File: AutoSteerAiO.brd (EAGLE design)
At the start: 114.3 x 99.1 mm, 82 parts, among them IC2 MMA8452Q, J4 CONNECTOR 1x5 PINS, K4 CB1A-P-12V

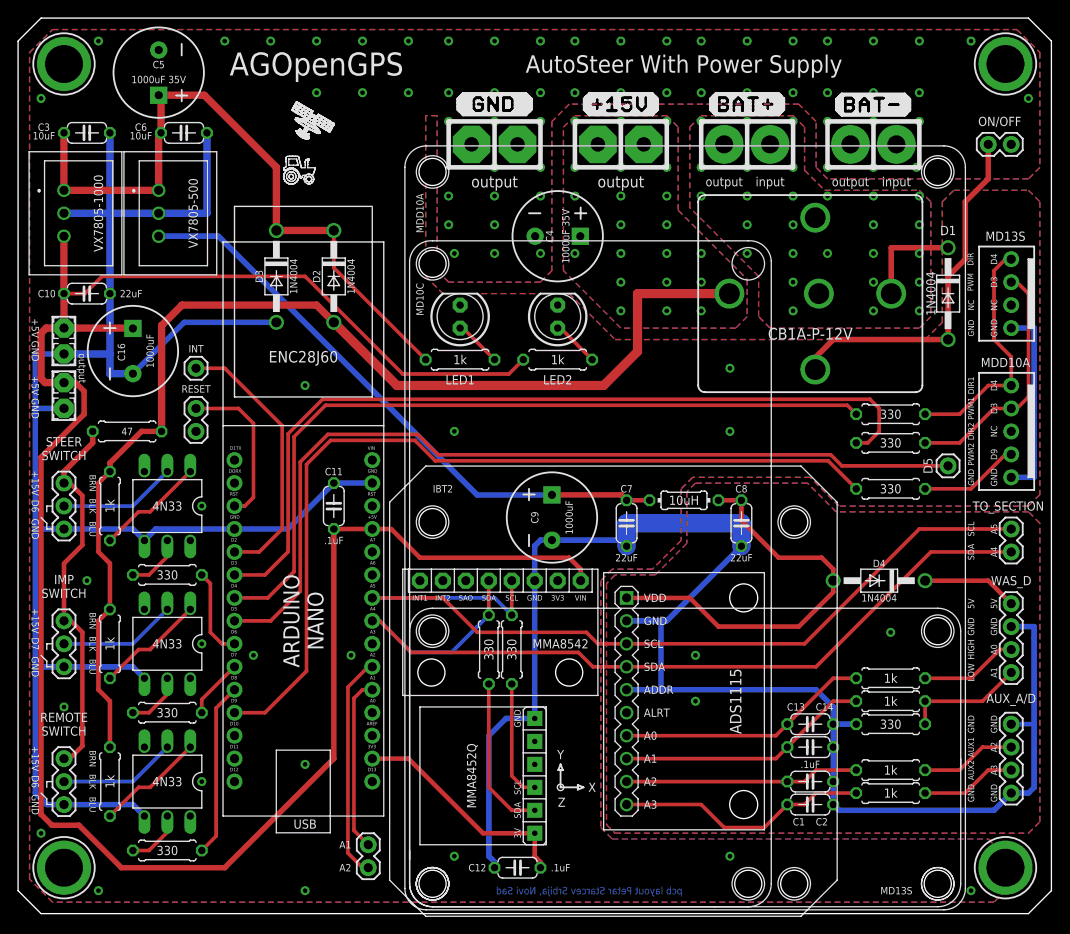
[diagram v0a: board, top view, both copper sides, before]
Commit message: Add files via upload
silkscreen
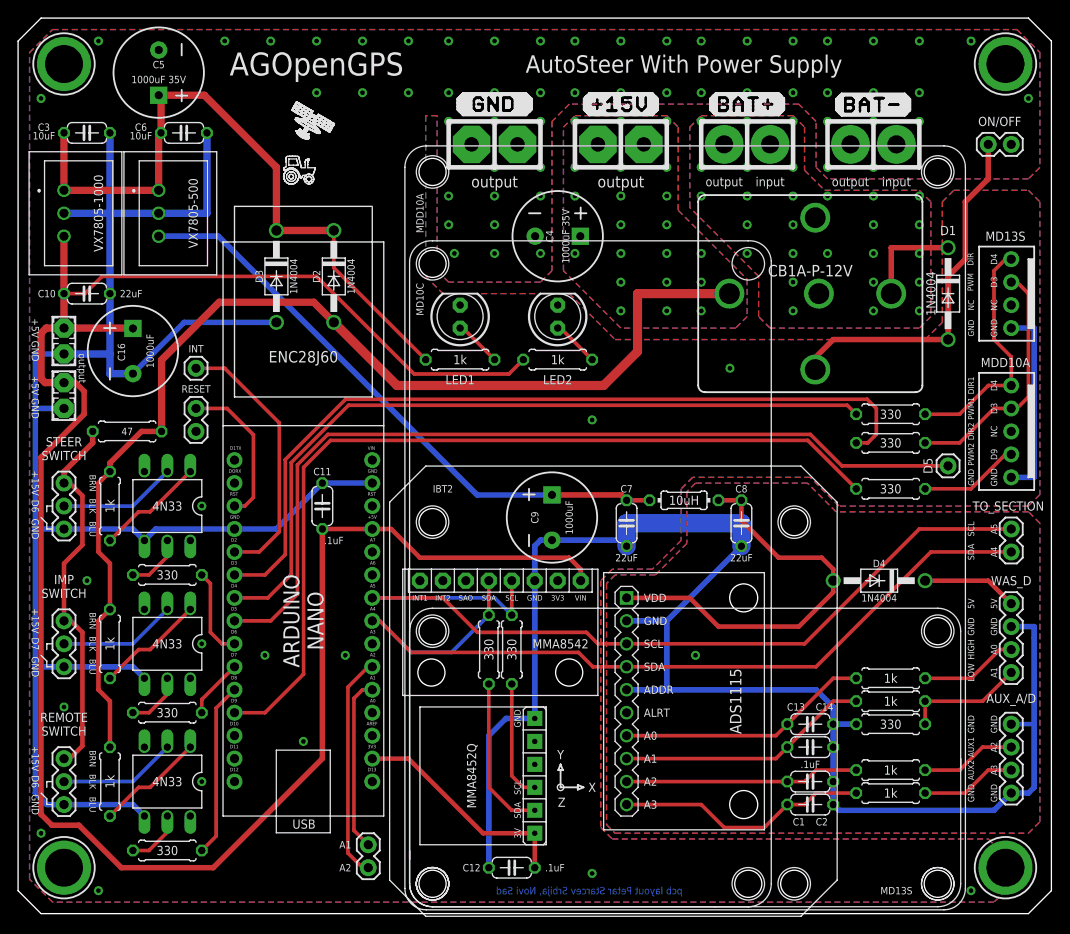
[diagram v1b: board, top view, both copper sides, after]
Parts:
- moved C11 1.27 mm to (33.7, 45.1)
- moved C12 0.63 mm to (54.6, 5.08)
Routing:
- net +15V: track 127.8 -> 125.8 mm
- net D3: track 93.0 -> 91.1 mm
- net D4: track 86.7 -> 85.3 mm
- net RST: track 17.7 -> 17.0 mm
- net GND: track 411.8 -> 411.6 mm, vias 78 -> 71

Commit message: Add files via upload
bottom silkscreen - edit
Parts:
- added U$11: SATELIT-MALI, #Logo:SATELIT-MALI
- added U$12: TRAKTOR-MALI, #Logo:TRAKTOR-MALI
- moved D2 6.35 mm to (34.9, 64.1)
- moved D3 6.35 mm to (28.6, 64.1)
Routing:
- net +15V: track 125.8 -> 121.6 mm
- net +5V: track 232.1 -> 228.9 mm
- net N$26: track 75.7 -> 77.0 mm
- net GND: track 411.6 -> 410.3 mm

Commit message: Add files via upload
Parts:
- removed PS2: VX7805-1000, #VX7805-500:VX7805500
- added U1: VX7805-1000, #VX7805-1000:VX78012-1000_VX7805-1000
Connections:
- net +5V: now also U1.3; no longer PS2.3
- net GND: now also U1.2; no longer PS2.2
- net N$26: now also U1.1; no longer PS2.1
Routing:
- net N$26: track 77.0 -> 81.0 mm
- net GND: track 410.3 -> 406.7 mm
- net +5V: track 228.9 -> 230.4 mm
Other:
- board text added: "VX7805-1000"

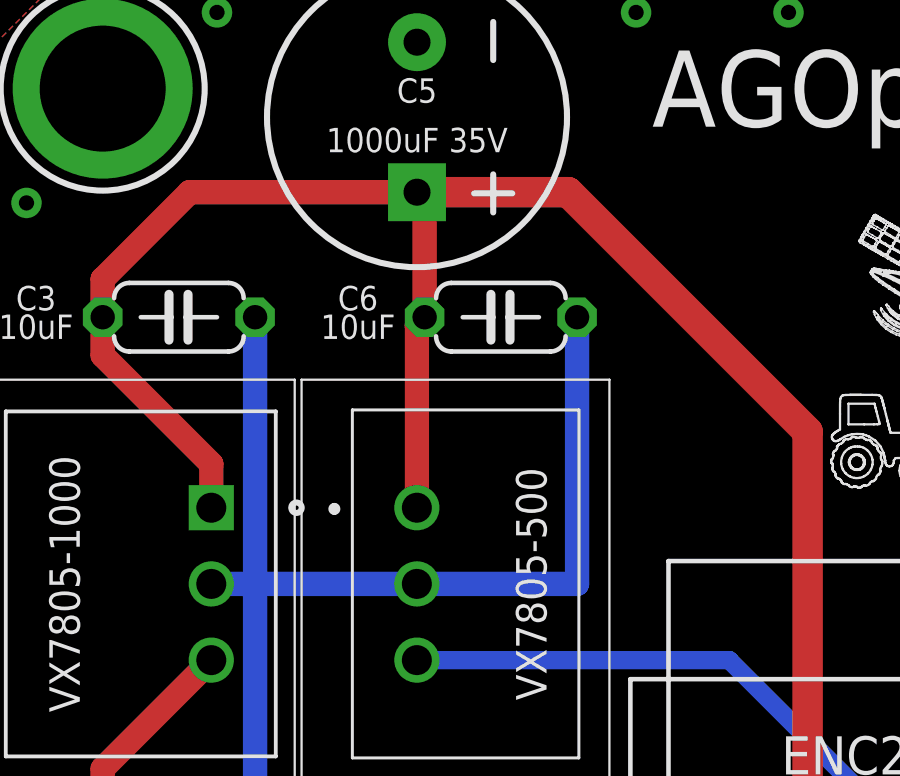
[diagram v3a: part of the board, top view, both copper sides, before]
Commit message: Add files via upload
wrong footprint VX7805-1000 it can fit but will come out with PCB
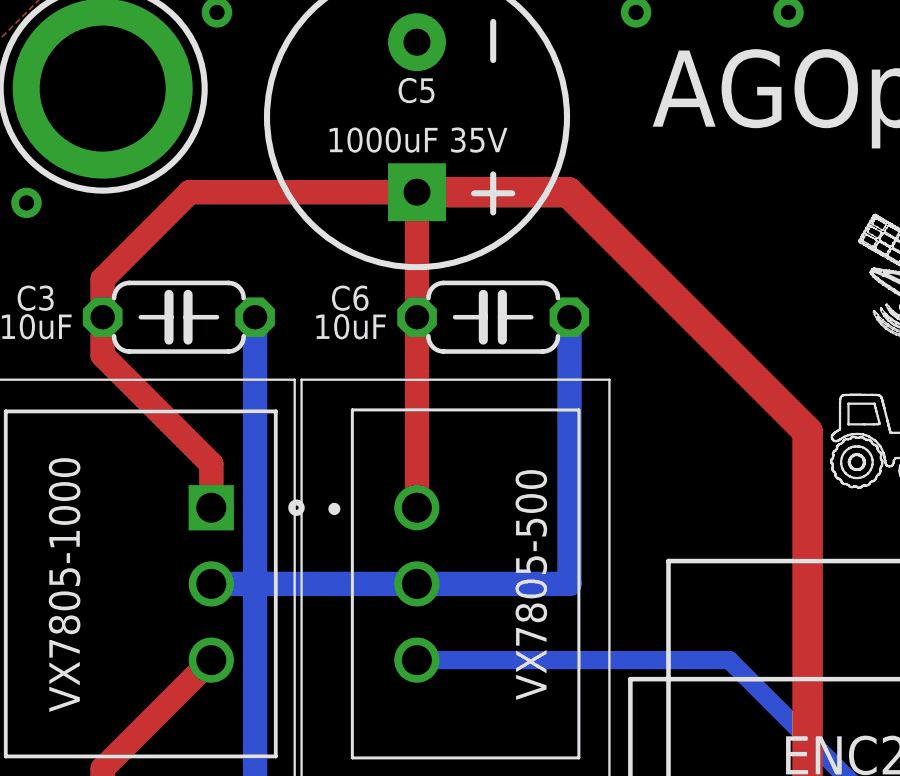
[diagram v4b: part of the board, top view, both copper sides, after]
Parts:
- moved C6 0.25 mm to (18.1, 86.4)
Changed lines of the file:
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@@
 <setting verticaltext="up"/>
 </settings>
-<grid distance="50" unitdist="mil" unit="mil" style="lines" multiple="1" display="no" altdistance="5" altunitdist="mil" altunit="mil"/>
+<grid distance="50" unitdist="mil" unit="mil" style="lines" multiple="1" display="yes" altdistance="12.5" altunitdist="mil" altunit="mil"/>
 <layers>
 <layer number="1" name="Top" color="4" fill="1" visible="yes" active="yes"/>
@@
 <attribute name="CYTRON-PC" value="CN-2600PS-05" x="109.855" y="48.26" size="1.778" layer="27" rot="R90" display="off"/>
 <attribute name="DESC" value="2600 PCB Connector" x="109.855" y="48.26" size="1.778" layer="27" rot="R90" display="off"/>
-<attribute name="LABEL" value="" x="112.776" y="46.863" size="0.762" layer="51" font="vector" ratio="15" rot="R90" align="top-left"/>
 <attribute name="LABEL" value="" x="112.776" y="46.863" size="0.762" layer="21" font="vector" ratio="15" rot="R90" align="top-left"/>
+<attribute name="LABEL" value="" x="112.776" y="46.863" size="0.762" layer="51" font="vector" ratio="15" rot="R90" align="top-left"/>
 <attribute name="LABEL" value="" x="109.855" y="48.26" size="1.778" layer="27" rot="R90" display="off"/>
 <attribute name="MF" value="" x="109.855" y="48.26" size="1.778" layer="27" rot="R90" display="off"/>
@@
 <attribute name="VALUE" x="80.01" y="39.37" size="0.8128" layer="25" font="vector" ratio="12" rot="R180" align="center"/>
 </element>
-<element name="C6" library="resistor" library_urn="urn:adsk.eagle:library:348" package="C050-024X044" package3d_urn="urn:adsk.eagle:package:23643/1" value="10uF" x="18.3515" y="86.36" smashed="yes" rot="R180">
-<attribute name="MF" value="" x="18.3515" y="86.36" size="1.778" layer="27" rot="R180" display="off"/>
-<attribute name="MPN" value="" x="18.3515" y="86.36" size="1.778" layer="27" rot="R180" display="off"/>
-<attribute name="NAME" x="13.589" y="86.995" size="0.8128" layer="25" font="vector" ratio="12" align="center"/>
-<attribute name="OC_NEWARK" value="unknown" x="18.3515" y="86.36" size="1.778" layer="27" rot="R180" display="off"/>
-<attribute name="VALUE" x="13.589" y="86.0425" size="0.8128" layer="25" font="vector" ratio="12" align="center"/>
+<element name="C6" library="resistor" library_urn="urn:adsk.eagle:library:348" package="C050-024X044" package3d_urn="urn:adsk.eagle:package:23643/1" value="10uF" x="18.0975" y="86.36" smashed="yes" rot="R180">
+<attribute name="MF" value="" x="18.0975" y="86.36" size="1.778" layer="27" rot="R180" display="off"/>
+<attribute name="MPN" value="" x="18.0975" y="86.36" size="1.778" layer="27" rot="R180" display="off"/>
+<attribute name="NAME" x="13.335" y="86.995" size="0.8128" layer="25" font="vector" ratio="12" align="center"/>
+<attribute name="OC_NEWARK" value="unknown" x="18.0975" y="86.36" size="1.778" layer="27" rot="R180" display="off"/>
+<attribute name="VALUE" x="13.335" y="86.0425" size="0.8128" layer="25" font="vector" ratio="12" align="center"/>
 </element>
 <element name="C10" library="resistor" library_urn="urn:adsk.eagle:library:348" package="C050-024X044" package3d_urn="urn:adsk.eagle:package:23643/1" value="22uF" x="7.62" y="68.58" smashed="yes" rot="R180">
@@
 <attribute name="DIGI-KEY_PART_NUMBER" value="102-4253-ND" x="6.35" y="77.47" size="1.778" layer="27" rot="R270" display="off"/>
 <attribute name="DIGI-KEY_PURCHASE_URL" value="https://www.digikey.rs/product-detail/en/cui-inc/VX7805-1000/102-4253-ND/7350292?utm_source=snapeda&amp;utm_medium=aggregator&amp;utm_campaign=symbol" x="6.35" y="77.47" size="1.778" layer="27" rot="R270" display="off"/>
-<attribute name="MF" value="CUI Inc." x="6.35" y="77.47" size="1.778" layer="27" rot="R270" display="off"/>
+<attribute name="MF" value="" x="6.35" y="77.47" size="1.778" layer="27" rot="R270" display="off"/>
 <attribute name="MP" value="VX7805-1000" x="6.35" y="77.47" size="1.778" layer="27" rot="R270" display="off"/>
+<attribute name="MPN" value="" x="6.35" y="77.47" size="1.778" layer="27" rot="R270" display="off"/>
+<attribute name="OC_NEWARK" value="unknown" x="6.35" y="77.47" size="1.778" layer="27" rot="R270" display="off"/>
 <attribute name="PACKAGE" value="SIP-3 CUI" x="6.35" y="77.47" size="1.778" layer="27" rot="R270" display="off"/>
 <attribute name="VALUE" x="-0.80181875" y="82.818840625" size="1.50248125" layer="27" rot="R270"/>
@@
 <contactref element="MMA8542" pad="GND"/>
 <wire x1="10.16" y1="77.47" x2="10.16" y2="68.58" width="0.8128" layer="16"/>
-<wire x1="20.8915" y1="86.36" x2="20.8915" y2="77.47" width="0.8128" layer="16"/>
-<wire x1="20.8915" y1="77.47" x2="15.5525" y2="77.47" width="0.8128" layer="16"/>
+<wire x1="20.6375" y1="86.36" x2="20.6375" y2="77.47" width="0.8128" layer="16"/>
+<wire x1="20.6375" y1="77.47" x2="15.5525" y2="77.47" width="0.8128" layer="16"/>
 <contactref element="STEER-SWITCH" pad="1"/>
 <contactref element="IMP-SWITCH" pad="1"/>
@@
 <contactref element="PS1" pad="1"/>
 <contactref element="C6" pad="2"/>
-<wire x1="15.8115" y1="86.36" x2="15.5525" y2="86.101" width="0.8128" layer="1"/>
-<wire x1="15.5525" y1="86.101" x2="15.5525" y2="80.01" width="0.8128" layer="1"/>
+<wire x1="15.5575" y1="86.36" x2="15.5575" y2="80.01" width="0.8128" layer="1"/>
+<wire x1="15.5575" y1="80.01" x2="15.555" y2="80.0125" width="0.8128" layer="1"/>
+<wire x1="15.555" y1="80.0125" x2="15.5525" y2="80.01" width="0.8128" layer="1"/>
 <wire x1="34.925" y1="69.215" x2="37.1475" y2="69.215" width="0.4064" layer="1"/>
 <wire x1="45.085" y1="61.2775" x2="37.1475" y2="69.215" width="0.4064" layer="1"/>
-<wire x1="15.8115" y1="86.36" x2="15.8115" y2="90.2735" width="0.8128" layer="1"/>
-<wire x1="15.8115" y1="90.2735" x2="15.5575" y2="90.5275" width="0.8128" layer="1"/>
+<wire x1="15.5575" y1="90.5275" x2="15.5575" y2="86.36" width="0.8128" layer="1"/>
 <contactref element="U1" pad="1"/>
 <wire x1="15.5575" y1="90.5275" x2="7.9775" y2="90.5275" width="0.8128" layer="1"/>

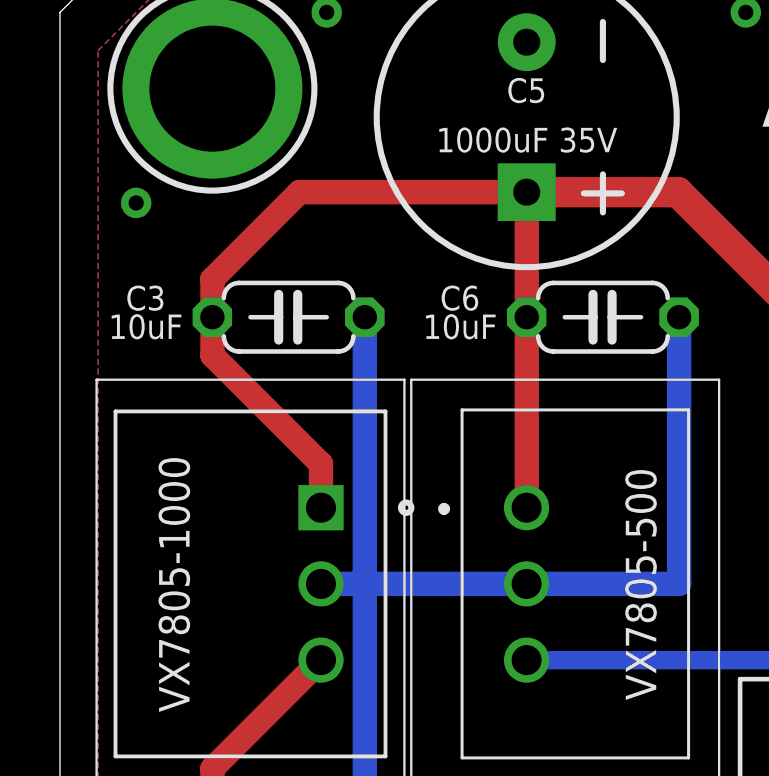
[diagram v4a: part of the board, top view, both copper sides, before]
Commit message: Add files via upload
wrong footprint VX7805-1000 it can fit, but will come out from PCB
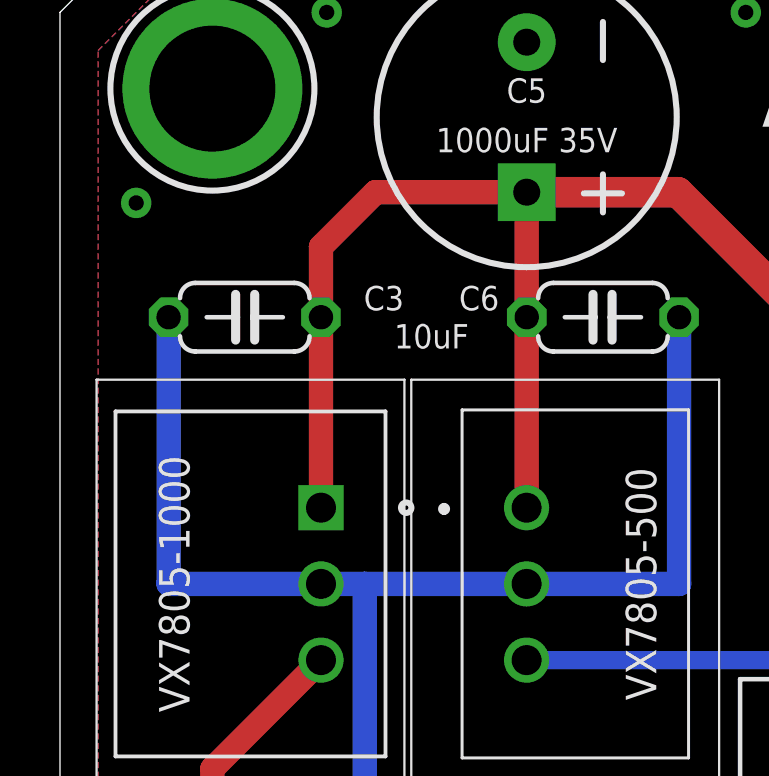
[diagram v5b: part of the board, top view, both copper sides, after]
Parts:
- moved C3 1.46 mm to (6.16, 86.4), turned to 0 degrees
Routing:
- net GND: track 406.4 -> 411.5 mm
- net N$26: track 80.8 -> 76.3 mm
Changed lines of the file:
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@@
 <drawing>
 <settings>
-<setting alwaysvectorfont="yes"/>
+<setting alwaysvectorfont="no"/>
 <setting keepoldvectorfont="yes"/>
 <setting verticaltext="up"/>
@@
 <attribute name="VALUE" x="48.895" y="61.2775" size="1.016" layer="25" font="vector" ratio="12" align="center"/>
 </element>
-<element name="C3" library="resistor" library_urn="urn:adsk.eagle:library:348" package="C050-024X044" package3d_urn="urn:adsk.eagle:package:23643/1" value="10uF" x="7.62" y="86.36" smashed="yes" rot="R180">
-<attribute name="MF" value="" x="7.62" y="86.36" size="1.778" layer="27" rot="R180" display="off"/>
-<attribute name="MPN" value="" x="7.62" y="86.36" size="1.778" layer="27" rot="R180" display="off"/>
-<attribute name="NAME" x="2.8575" y="86.995" size="0.8128" layer="25" font="vector" ratio="12" align="center"/>
-<attribute name="OC_NEWARK" value="unknown" x="7.62" y="86.36" size="1.778" layer="27" rot="R180" display="off"/>
-<attribute name="VALUE" x="2.8575" y="86.0425" size="0.8128" layer="25" font="vector" ratio="12" align="center"/>
+<element name="C3" library="resistor" library_urn="urn:adsk.eagle:library:348" package="C050-024X044" package3d_urn="urn:adsk.eagle:package:23643/1" value="10uF" x="6.1595" y="86.36" smashed="yes">
+<attribute name="MF" value="" x="6.1595" y="86.36" size="1.778" layer="27" display="off"/>
+<attribute name="MPN" value="" x="6.1595" y="86.36" size="1.778" layer="27" display="off"/>
+<attribute name="NAME" x="10.795" y="86.995" size="0.8128" layer="25" font="vector" ratio="12" rot="R180" align="center"/>
+<attribute name="OC_NEWARK" value="unknown" x="6.1595" y="86.36" size="1.778" layer="27" display="off"/>
 </element>
 <element name="LED2" library="adafruit" library_urn="urn:adsk.eagle:library:420" package="LED5MM" package3d_urn="urn:adsk.eagle:package:6240538/1" value="LED" x="59.69" y="66.04" smashed="yes" rot="R90">
@@
 <attribute name="MF" value="" x="18.0975" y="86.36" size="1.778" layer="27" rot="R180" display="off"/>
 <attribute name="MPN" value="" x="18.0975" y="86.36" size="1.778" layer="27" rot="R180" display="off"/>
-<attribute name="NAME" x="13.335" y="86.995" size="0.8128" layer="25" font="vector" ratio="12" align="center"/>
+<attribute name="NAME" x="13.97" y="86.995" size="0.8128" layer="25" font="vector" ratio="12" align="center"/>
 <attribute name="OC_NEWARK" value="unknown" x="18.0975" y="86.36" size="1.778" layer="27" rot="R180" display="off"/>
-<attribute name="VALUE" x="13.335" y="86.0425" size="0.8128" layer="25" font="vector" ratio="12" align="center"/>
+<attribute name="VALUE" x="12.3825" y="85.725" size="0.8128" layer="25" font="vector" ratio="12" align="center"/>
 </element>
 <element name="C10" library="resistor" library_urn="urn:adsk.eagle:library:348" package="C050-024X044" package3d_urn="urn:adsk.eagle:package:23643/1" value="22uF" x="7.62" y="68.58" smashed="yes" rot="R180">
@@
 <contactref element="C10" pad="1"/>
 <via x="52.705" y="90.805" extent="1-16" drill="0.508"/>
-<wire x1="10.16" y1="86.36" x2="10.16" y2="77.47" width="0.8128" layer="16"/>
 <contactref element="MMA8542" pad="GND"/>
 <wire x1="10.16" y1="77.47" x2="10.16" y2="68.58" width="0.8128" layer="16"/>
@@
 <wire x1="15.5525" y1="77.47" x2="10.16" y2="77.47" width="0.8128" layer="16"/>
 <wire x1="10.16" y1="77.47" x2="8.7" y2="77.47" width="0.8128" layer="16"/>
+<wire x1="3.6195" y1="86.36" x2="3.6195" y2="77.47" width="0.8128" layer="16"/>
+<wire x1="3.6195" y1="77.47" x2="8.7" y2="77.47" width="0.8128" layer="16"/>
 </signal>
 <signal name="D5">
@@
 <wire x1="15.5575" y1="90.5275" x2="15.5575" y2="86.36" width="0.8128" layer="1"/>
 <contactref element="U1" pad="1"/>
-<wire x1="15.5575" y1="90.5275" x2="7.9775" y2="90.5275" width="0.8128" layer="1"/>
-<wire x1="7.9775" y1="90.5275" x2="5.08" y2="87.63" width="0.8128" layer="1"/>
-<wire x1="5.08" y1="87.63" x2="5.08" y2="86.36" width="0.8128" layer="1"/>
-<wire x1="8.7" y1="81.47" x2="5.08" y2="85.09" width="0.8128" layer="1"/>
-<wire x1="5.08" y1="86.36" x2="5.08" y2="85.09" width="0.8128" layer="1"/>
-<wire x1="8.7" y1="81.47" x2="8.7" y2="80.01" width="0.8128" layer="1"/>
+<wire x1="15.5575" y1="90.5275" x2="10.5175" y2="90.5275" width="0.8128" layer="1"/>
+<wire x1="10.5175" y1="90.5275" x2="8.6995" y2="88.7095" width="0.8128" layer="1"/>
+<wire x1="8.6995" y1="88.7095" x2="8.6995" y2="86.36" width="0.8128" layer="1"/>
+<wire x1="8.6995" y1="86.36" x2="8.7" y2="86.3595" width="0.8128" layer="1"/>
+<wire x1="8.7" y1="86.3595" x2="8.7" y2="80.01" width="0.8128" layer="1"/>
 <wire x1="34.925" y1="69.215" x2="28.575" y2="69.215" width="1.016" layer="1"/>
 <wire x1="28.575" y1="69.215" x2="28.575" y2="82.55" width="1.016" layer="1"/>
